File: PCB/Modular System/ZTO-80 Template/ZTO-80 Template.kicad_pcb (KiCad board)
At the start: 2 copper layers, 99.1 x 57.1 mm, 6 parts, among them J1 ZTO-80 Bus, J2 Conn_01x02

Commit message: Edited power LED resistor value
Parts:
- R1: value 200 -> 220

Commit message: Edit READMEs
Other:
- board text added: "SEE THE README FOR MORE INFO AND DESIGN CONSIDERATIONS"
- board text removed: "READ EXPLANATORY DOC FOR MORE INFO AND DESIGN CONSIDERATIONS"
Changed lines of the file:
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@@
-(kicad_pcb (version 20171130) (host pcbnew "(5.1.6)-1")
+(kicad_pcb (version 20171130) (host pcbnew "(5.1.5)-3")
   (general
     (thickness 1.6)
@@
   )
   (gr_line (start 95.885 120.015) (end 95.885 62.865) (layer Dwgs.User) (width 0.15))
-  (gr_text "READ EXPLANATORY DOC FOR MORE INFO\nAND DESIGN CONSIDERATIONS" (at 145.415 65.405) (layer Cmts.User)
+  (gr_text "SEE THE README FOR MORE INFO\nAND DESIGN CONSIDERATIONS" (at 145.415 65.405) (layer Cmts.User)
     (effects (font (size 1.27 1.27) (thickness 0.15)))
   )

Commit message: Updates to PDFs and the SBC
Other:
- board text added: "BACK: PLACE OUTPUT HEADERS ALONG THIS EDGE"
- board text added: "COMPONENT KEEPOUT FOR ENCLOSURE COMPATIBILITY (.0985 IN. WIDE, FRONT AND BACK):"
- board text added: "VERSION DESIGNER AND YEAR:"
- board text added: "ZTO-80 TEMPLATE"
- board text added: "v1.1"
- board text removed: "BACK"
- board text removed: "BACK INDICATOR (REAR): PLACE OUTPUT HEADERS ON THIS EDGE"
- board text removed: "COMPONENT KEEPOUT FOR ENCLOSURE COMPATIBILITY (.0985 IN. WIDE):"
- board text removed: "DESIGNER AND YEAR:"
- board text removed: "ZTO-80 TEMPLATE V1.0"
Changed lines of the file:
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@@
     )
+  )
+  (gr_text v1.1 (at 172.085 115.57) (layer F.SilkS)
+    (effects (font (size 1.524 1.524) (thickness 0.2032)) (justify left))
   )
   (gr_line (start 95.885 120.015) (end 95.885 62.865) (layer Dwgs.User) (width 0.15))
@@
     (effects (font (size 1.27 1.27) (thickness 0.15)))
   )
-  (gr_text "COMPONENT KEEPOUT\nFOR ENCLOSURE \nCOMPATIBILITY\n(.0985 IN. WIDE):" (at 94.615 90.805) (layer Dwgs.User)
+  (gr_text "COMPONENT KEEPOUT\nFOR ENCLOSURE \nCOMPATIBILITY\n(.0985 IN. WIDE,\nFRONT AND BACK):" (at 94.615 90.805) (layer Dwgs.User)
     (effects (font (size 1 1) (thickness 0.15)) (justify right))
   )
@@
   (gr_line (start 98.3869 62.865) (end 98.3869 120.015) (layer Dwgs.User) (width 0.15))
   (gr_line (start 95.885 62.865) (end 98.3869 62.865) (layer Dwgs.User) (width 0.15))
-  (gr_text "BACK INDICATOR (REAR):\nPLACE OUTPUT\nHEADERS ON \nTHIS EDGE" (at 190.5 91.44) (layer Cmts.User)
+  (gr_text "BACK:\nPLACE OUTPUT\nHEADERS ALONG\nTHIS EDGE" (at 193.675 90.805) (layer Cmts.User)
     (effects (font (size 1.27 1.27) (thickness 0.15)) (justify right))
   )
@@
     (effects (font (size 1.27 1.27) (thickness 0.15)))
   )
-  (gr_text "DESIGNER AND YEAR:" (at 182.245 115.57) (layer Cmts.User)
-    (effects (font (size 1.27 1.27) (thickness 0.15)))
+  (gr_text "VERSION\nDESIGNER AND YEAR:" (at 172.085 112.395) (layer Cmts.User)
+    (effects (font (size 1.27 1.27) (thickness 0.15)) (justify left))
   )
   (gr_text POWER (at 101.6 73.025) (layer F.SilkS)
@@
     (effects (font (size 1.27 1.27) (thickness 0.15)))
   )
-  (gr_text "MODULE TITLE:" (at 123.19 106.045) (layer Cmts.User)
+  (gr_text "MODULE TITLE:" (at 127.635 106.68) (layer Cmts.User)
     (effects (font (size 1.27 1.27) (thickness 0.15)) (justify left))
-  )
-  (gr_text BACK (at 193.04 91.44 90) (layer B.SilkS)
-    (effects (font (size 2.032 2.032) (thickness 0.2032)) (justify mirror))
   )
   (gr_text JLCJLCJLCJLC (at 189.865 118.745) (layer B.SilkS)
@@
     (effects (font (size 1.524 1.524) (thickness 0.2032)))
   )
-  (gr_text "ZTO-80 TEMPLATE V1.0" (at 145.415 109.22) (layer F.SilkS)
+  (gr_text "ZTO-80 TEMPLATE" (at 145.415 109.855) (layer F.SilkS)
     (effects (font (size 2.54 2.54) (thickness 0.254)))
   )

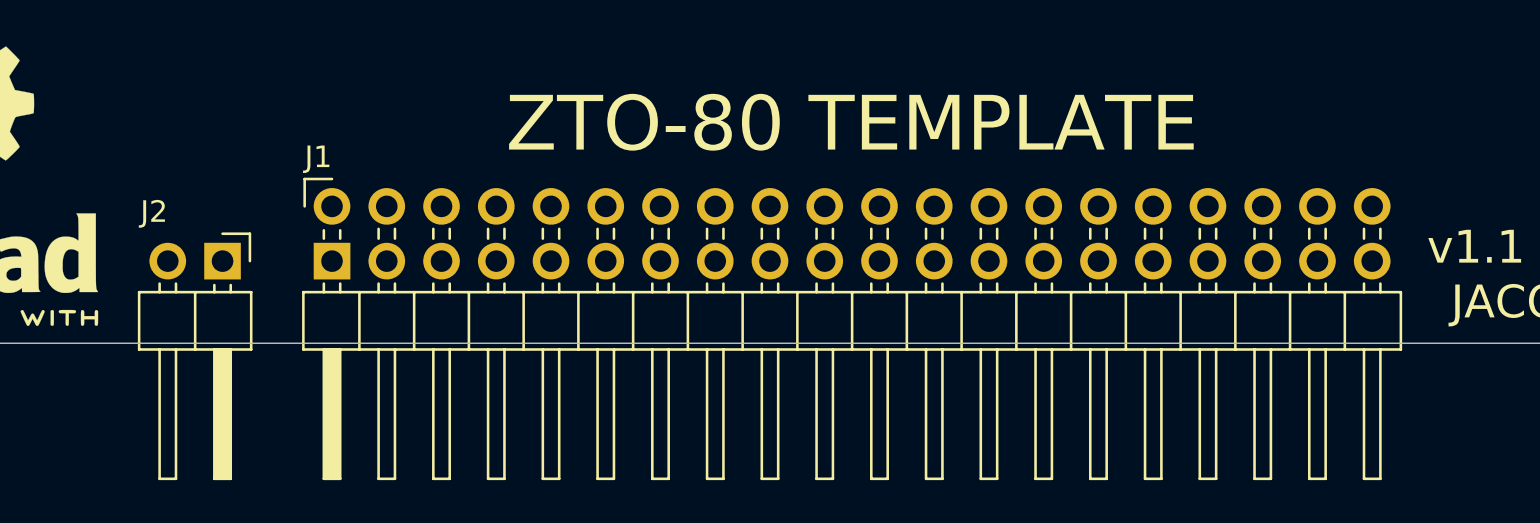
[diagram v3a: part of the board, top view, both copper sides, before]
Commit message: Changed bus orientation
This change is backwards-compatible with all previous ZTO-80 modules
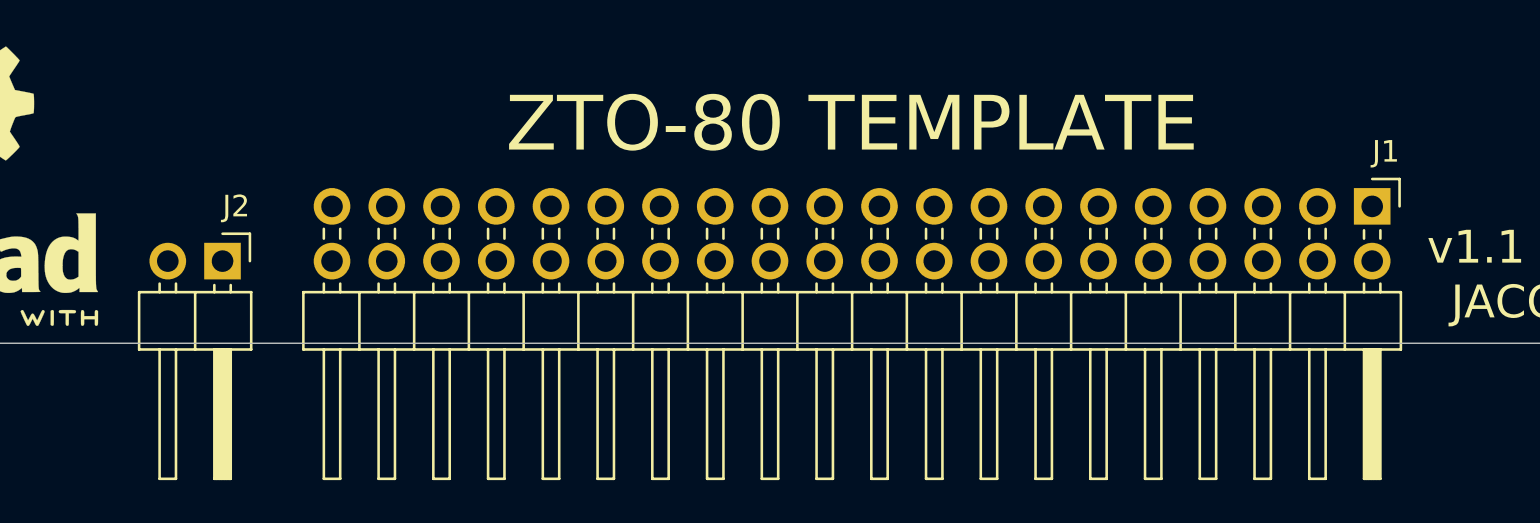
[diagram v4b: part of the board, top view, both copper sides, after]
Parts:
- J1: footprint ZTO-80_Header:PinHeader_2x20_P2.54mm_Horizontal -> Connector_PinHeader_2.54mm:PinHeader_2x20_P2.54mm_Horizontal
- moved J1 48.3 mm to (169.5, 113.7), turned to 270 degrees
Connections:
- J1 pad 1: /A15 -> /USR4
- J1 pad 10: /A6 -> /MREQ
- J1 pad 11: /A5 -> /INT
- J1 pad 12: /A4 -> /RST
- J1 pad 13: /A3 -> /M1
- J1 pad 14: /A2 -> /CLK
- J1 pad 15: /A1 -> /D0
- J1 pad 16: /A0 -> /D1
- J1 pad 17: VCC -> /D2
- J1 pad 18: GND -> /D3
- J1 pad 19: /D7 -> /D4
- J1 pad 2: /A14 -> /USR3
- J1 pad 20: /D6 -> /D5
- J1 pad 21: /D5 -> /D6
- J1 pad 22: /D4 -> /D7
- J1 pad 23: /D3 -> GND
- J1 pad 24: /D2 -> VCC
- J1 pad 25: /D1 -> /A0
- J1 pad 26: /D0 -> /A1
- J1 pad 27: /CLK -> /A2
- J1 pad 28: /M1 -> /A3
- J1 pad 29: /RST -> /A4
- J1 pad 3: /A13 -> /USR2
- J1 pad 30: /INT -> /A5
- J1 pad 31: /MREQ -> /A6
- J1 pad 32: /WR -> /A7
- J1 pad 33: /IORQ -> /A8
- J1 pad 34: /RD -> /A9
- J1 pad 35: /TXB -> /A10
- J1 pad 36: /RXB -> /A11
- J1 pad 37: /USR1 -> /A12
- J1 pad 38: /USR2 -> /A13
- J1 pad 39: /USR3 -> /A14
- J1 pad 4: /A12 -> /USR1
- J1 pad 40: /USR4 -> /A15
- J1 pad 5: /A11 -> /RXB
- J1 pad 6: /A10 -> /TXB
- J1 pad 7: /A9 -> /RD
- J1 pad 8: /A8 -> /IORQ
- J1 pad 9: /A7 -> /WR

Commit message: Added CERN license text to silkscreen
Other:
- board text added: "Licensed under CERN-OHL-S v2"
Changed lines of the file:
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@@
   (general
     (thickness 1.6)
-    (drawings 66)
+    (drawings 67)
     (tracks 0)
     (zones 0)
@@
     )
   )
+  (gr_text "Licensed under CERN-OHL-S v2" (at 109.22 118.745) (layer B.SilkS)
+    (effects (font (size 1 1) (thickness 0.15)) (justify mirror))
+  )
   (gr_text v1.1 (at 172.085 115.57) (layer F.SilkS)
